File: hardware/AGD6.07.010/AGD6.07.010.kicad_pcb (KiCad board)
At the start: 4 copper layers, 90 x 130 mm, 286 parts, among them J1001 PX_ETH GH4, J1002 SIYI_ETH GH4, J1003 CAMF_ETH GH4, J1004 AI_ETH1 GH4, J1005 SERVICE_ETH GH4, J1006 AI_ETH2 GH4, J1007 ETH_SWITCH_MODULE 2x13, J1008 CAMD_ETH GH4, J101 PDB_14S XT30, J202 AI_POWER_12V XT30, J301 PX_CAN1 GH4, J302 PX_CAN2 GH4, J303 PX_TELEM1 SIYI GH6, J304 PX_TELEM2 AI GH6, J305 PX_TELEM3 RADAR GH6, J306 PX_I2C GH4, J307 PX_AD&IO GH8, J308 PX_RC_IN GH3, J309 PX_MAIN 1-8, J310 PX_AUX 1-8, J311 FTS GH3, J312 MODE_SWITCH + LID/BATT_LATCH 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, J401 CAN1 ESC CHAIN START GH4, J402 CAN1 ESC CHAIN RETURN GH4, J407 PM08-CAN GH4, J408 BMS CAN GH4, J409 REMOTE_ID GH4, J410 GNSS2 (резерв) GH4, J411 OBSTACLE_1 GH4, J412 OBSTACLE_2 GH4, J413 SPRAY_SENSORS GH8 (давл./уров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, J421 ESC1-6 PWM backup GH8, J501 SIYI_PWR XT30, J502 SIYI_DATA GH5, J503 RADAR_US-D1 GH4, J504 GNSS_PPS GH2, J601 AI_SIGNALS GH8, J602 AI_OFF_SWITCH GH2, J603 SERVICE USB-C, J604 AI_USB GH4, J701 TEMP_AI_HEATSINK GH4, J702 TEMP_AIR GH4, J801 VALVE1 XH2, J802 VALVE2 XH2, J803 LIGHTS XH2, J804 FAN XH2, J805 HEATER XH2, J806 PUMP_PWM + CAM_TRIG GH4, J901 CAM_FRONT_PWR XH2, J902 CAM_DOWN_PWR XH2, Q101 100V N-MOSFET >=40A D2PAK (на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, Q201 40V N-MOSFET >=40A D2PAK (нап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, Q801 AO3400A, Q802 AO3401A, Q803 AO3400A, Q804 AO3400A, U101 LM5069MM-1, U102 INA228AIDGSR, U201 TPS62133RGTR, U202 AP2112K-3.3TRG1, U203 LM5069MM-2, U204 INA228AIDGSR, U205 INA228AIDGSR, U501 TPD4E05U06DQA, U502 TPD4E05U06DQA, U602 TPD4E05U06DQA, U603 USBLC6-2SC6, U701 TPS3430WDRC, U702 TMP117AIDRVR, U703 SHT40-AD1B, U704 TPD4E05U06DQA, U801 BTS5030-1EJA, U802 BTS5030-1EJA, U803 BTS5030-1EJA, U804 ADS1115IDGSR

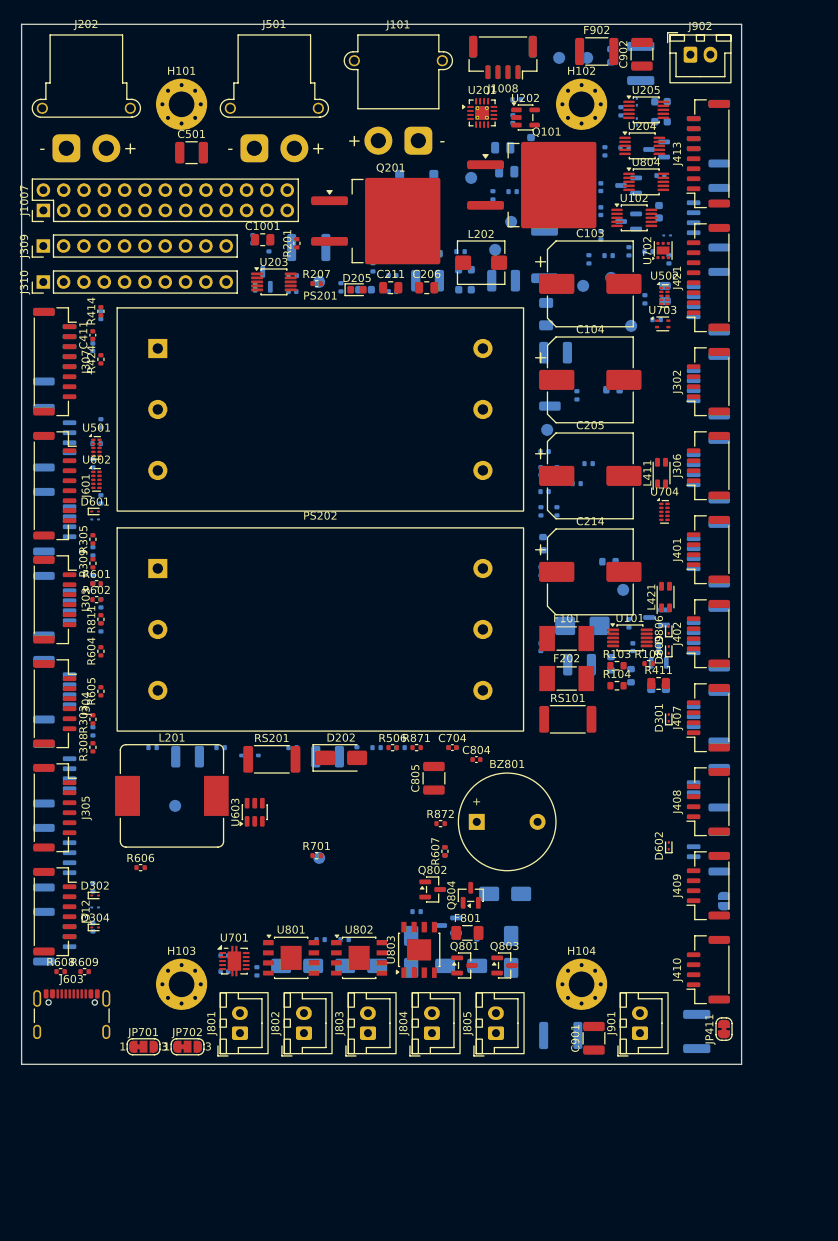
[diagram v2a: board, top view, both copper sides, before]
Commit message: AGD6.07.010: enlarge board to 100x150 mm and re-place
Board size raised within the allowed 30 % (area +28 %), M3 pattern
kept at 50 x 110 mm centred. All 286 parts re-placed, every connector
on a board edge; schematic parity clean. Routing in progress.

Co-Authored-By: Claude Opus 5.5 <noreply@anthropic.com>
Claude-Session: https://claude.ai/code/session_01Qk7uTKdi6YbndB9fGuguYV
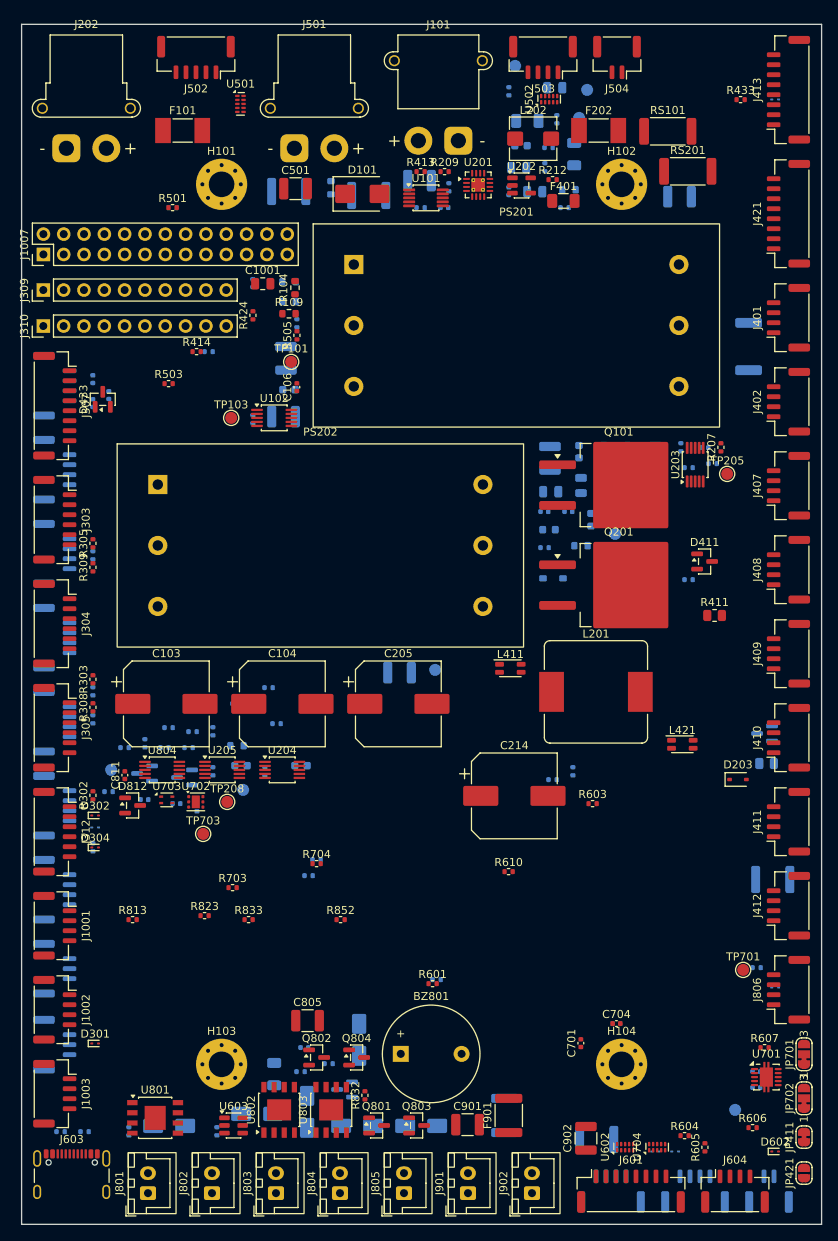
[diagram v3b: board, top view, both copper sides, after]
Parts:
- C106, C701, C811, D101, D203, D411, D433, D812, F401, F901, J1001, J1002, J1003, J411, J412, J502, J503, J504, J604, J806, JP421, R109, R209, R212, R302, R413, R433, R501, R503, R505, R603, R610, R703, R704, R813, R823, R832, R833, R852, TP101, TP103, TP205, TP208, TP701, TP703: moved to F.Cu
- C206, C211, C411, C804, D202, D205, D601, D806, D809, F801, F902, J1008, J302, J306, R103, R106, R201, R506, R602, R608, R609, R701, R811, R871, R872: moved to B.Cu
- moved J902 143.7 mm to (163.8, 196.1), turned to 90 degrees
- moved F902 136.0 mm to (171.9, 189.4), turned to 180 degrees
- moved C902 135.7 mm to (170.5, 189.2)
- moved J601 113.9 mm to (176.2, 195.9), turned to 0 degrees
- moved D603 107.2 mm to (181.7, 190.9)
- moved U602 106.4 mm to (175.4, 190.4), turned to 90 degrees
- moved D601 106.3 mm to (179.2, 190.9), turned to 180 degrees
- moved F402 103.3 mm to (193.9, 156.9), turned to 180 degrees
- moved TP208 101.8 mm to (125.7, 147.2), turned to 0 degrees
- moved TP206 101.1 mm to (127.7, 145.7)
- moved J604 100.7 mm to (189.2, 195.9), turned to 0 degrees
- moved J301 100.2 mm to (104.1, 137.2), turned to 90 degrees
- moved C831 99.1 mm to (119.4, 147.4)
- moved C217 98.2 mm to (127.4, 142.7)
- moved D813 98.2 mm to (120.4, 144.1)
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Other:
- board size 90 x 130 mm -> 100 x 150 mm

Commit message: AGD6.07.010: first routing pass and power pours on outer layers
Freerouting pass 1 on the 100x150 mm board. Power nets (14S, AI 12 V,
12 V) moved off the inner layer into solid-connected pours on the 2 oz
outer layers per the IPC-2221 width calculation. Remaining connections
are being completed by a second autorouter pass.

Co-Authored-By: Claude Opus 5.5 <noreply@anthropic.com>
Claude-Session: https://claude.ai/code/session_01Qk7uTKdi6YbndB9fGuguYV
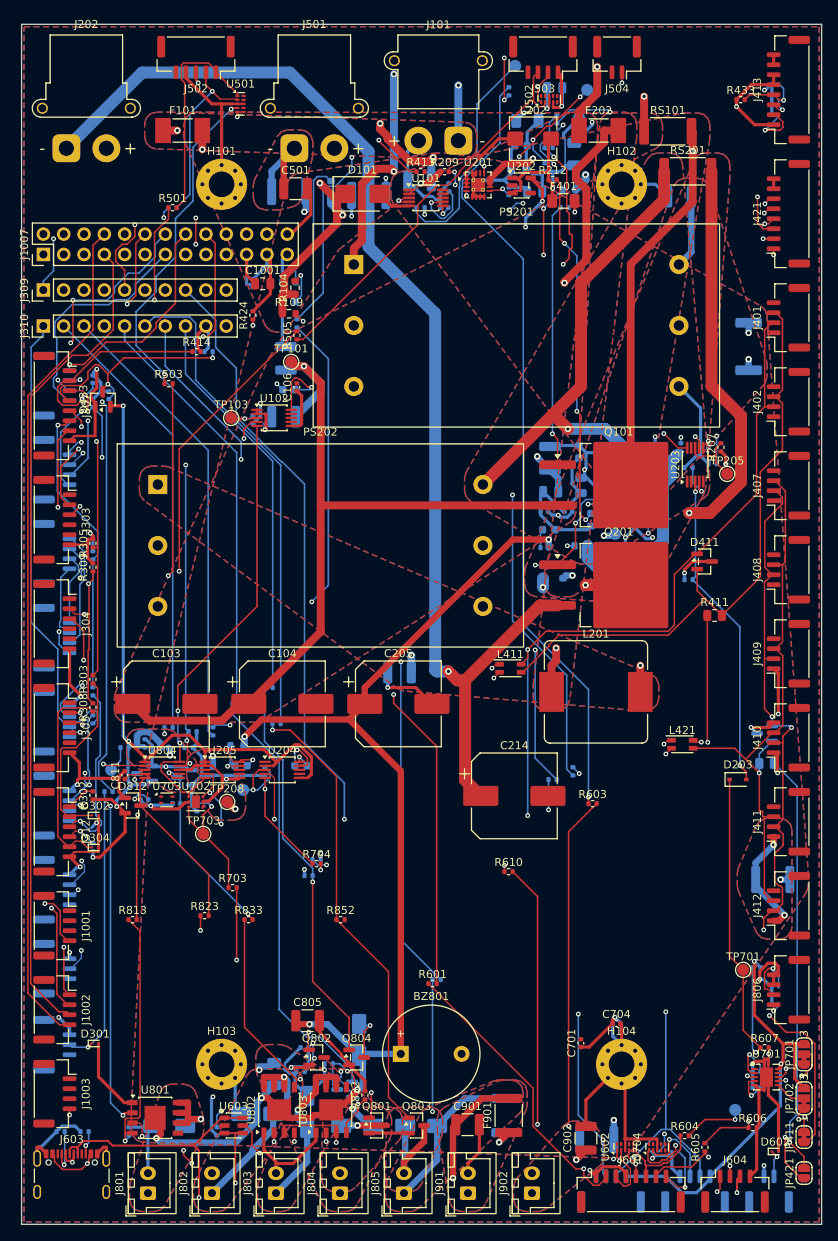
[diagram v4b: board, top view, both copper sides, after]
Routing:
- net +3V3: track 0.00 -> 510.7 mm, vias 0 -> 18
- net GND: track 0.00 -> 436.7 mm, vias 0 -> 25
- net +12V: track 0.00 -> 190.9 mm, vias 0 -> 16
- net /CAN_AND_SENSORS/C1H: track 0.00 -> 151.0 mm, vias 0 -> 3
- net /POWER_CONVERSION/V12_AI: track 0.00 -> 149.0 mm, vias 0 -> 1
- net /VIN_PROT: track 0.00 -> 141.9 mm, vias 0 -> 4
- net /ESC_PWM1: track 0.00 -> 120.0 mm, vias 0 -> 2
- net /ETHERNET/E3_RXN: track 0.00 -> 119.6 mm, vias 0 -> 2
- net /I2C_SCL: track 0.00 -> 119.5 mm, vias 0 -> 4
- net /CAN_AND_SENSORS/C2H: track 0.00 -> 113.7 mm, vias 0 -> 5
- net /ESC_PWM2: track 0.00 -> 113.0 mm, vias 0 -> 1
- net /I2C_SDA: track 0.00 -> 109.9 mm, vias 0 -> 9
- net /ADC_LEVEL: track 0.00 -> 107.1 mm, vias 0 -> 5
- net /ESC_PWM3: track 0.00 -> 106.5 mm, vias 0 -> 1
- net /ETHERNET/E2_RXN: track 0.00 -> 105.7 mm
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- added copper zone on B.Cu, net +12V
- added copper zone on F.Cu, net +12V
- added copper zone on B.Cu, net /CAMERAS/V12_CAMD
- added copper zone on F.Cu, net /CAMERAS/V12_CAMD
- added copper zone on B.Cu, net /CAMERAS/V12_CAMF
- added copper zone on F.Cu, net /CAMERAS/V12_CAMF
- added copper zone on B.Cu, net /CAN_AND_SENSORS/V12_OBST
- added copper zone on F.Cu, net /CAN_AND_SENSORS/V12_OBST
- added copper zone on B.Cu, net /LOAD_SWITCHES_12V/FAN_N
- added copper zone on F.Cu, net /LOAD_SWITCHES_12V/FAN_N
- added copper zone on B.Cu, net /LOAD_SWITCHES_12V/HEAT_N
- added copper zone on F.Cu, net /LOAD_SWITCHES_12V/HEAT_N
- added copper zone on B.Cu, net /LOAD_SWITCHES_12V/OUT1
- added copper zone on F.Cu, net /LOAD_SWITCHES_12V/OUT1
- added copper zone on B.Cu, net /LOAD_SWITCHES_12V/OUT2
- added copper zone on F.Cu, net /LOAD_SWITCHES_12V/OUT2
- added copper zone on B.Cu, net /LOAD_SWITCHES_12V/OUT3
- added copper zone on F.Cu, net /LOAD_SWITCHES_12V/OUT3
- added copper zone on B.Cu, net /LOAD_SWITCHES_12V/V12_FAN
- added copper zone on F.Cu, net /LOAD_SWITCHES_12V/V12_FAN
- added copper zone on B.Cu, net /LOAD_SWITCHES_12V/V12_HEAT
- added copper zone on F.Cu, net /LOAD_SWITCHES_12V/V12_HEAT
- added copper zone on B.Cu, net /LOAD_SWITCHES_12V/V12_MON
- added copper zone on F.Cu, net /LOAD_SWITCHES_12V/V12_MON
- added copper zone on B.Cu, net /POWER_CONVERSION/AI_SNS
- added copper zone on F.Cu, net /POWER_CONVERSION/AI_SNS
- added copper zone on B.Cu, net /POWER_CONVERSION/V12AI_RAW
- added copper zone on F.Cu, net /POWER_CONVERSION/V12AI_RAW
- added copper zone on B.Cu, net /POWER_CONVERSION/V12_ALERT_N
- added copper zone on F.Cu, net /POWER_CONVERSION/V12_ALERT_N
- added copper zone on B.Cu, net /POWER_CONVERSION/V12_RAW
- added copper zone on F.Cu, net /POWER_CONVERSION/V12_RAW
- added copper zone on B.Cu, net /POWER_CONVERSION/VIN_AI
- added copper zone on F.Cu, net /POWER_CONVERSION/VIN_AI
- added copper zone on B.Cu, net /POWER_CONVERSION/VIN_AI_F
- added copper zone on F.Cu, net /POWER_CONVERSION/VIN_AI_F
- added copper zone on B.Cu, net /POWER_INPUT_14S/SNS
- added copper zone on F.Cu, net /POWER_INPUT_14S/SNS
- added copper zone on B.Cu, net /POWER_INPUT_14S/VIN_F
- added copper zone on F.Cu, net /POWER_INPUT_14S/VIN_F
- added copper zone on B.Cu, net /POWER_INPUT_14S/VIN_RAW
- added copper zone on F.Cu, net /POWER_INPUT_14S/VIN_RAW
- added copper zone on B.Cu, net /RC_AND_TELEMETRY/V12_SIYI
- added copper zone on F.Cu, net /RC_AND_TELEMETRY/V12_SIYI
- added copper zone on B.Cu, net /VIN_PROT
- added copper zone on F.Cu, net /VIN_PROT
- added copper zone on B.Cu, net GND
- added copper zone on F.Cu, net GND
